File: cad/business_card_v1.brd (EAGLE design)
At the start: 50 x 50 mm, 31 parts, among them SW1 SPST_TACT-KMR2

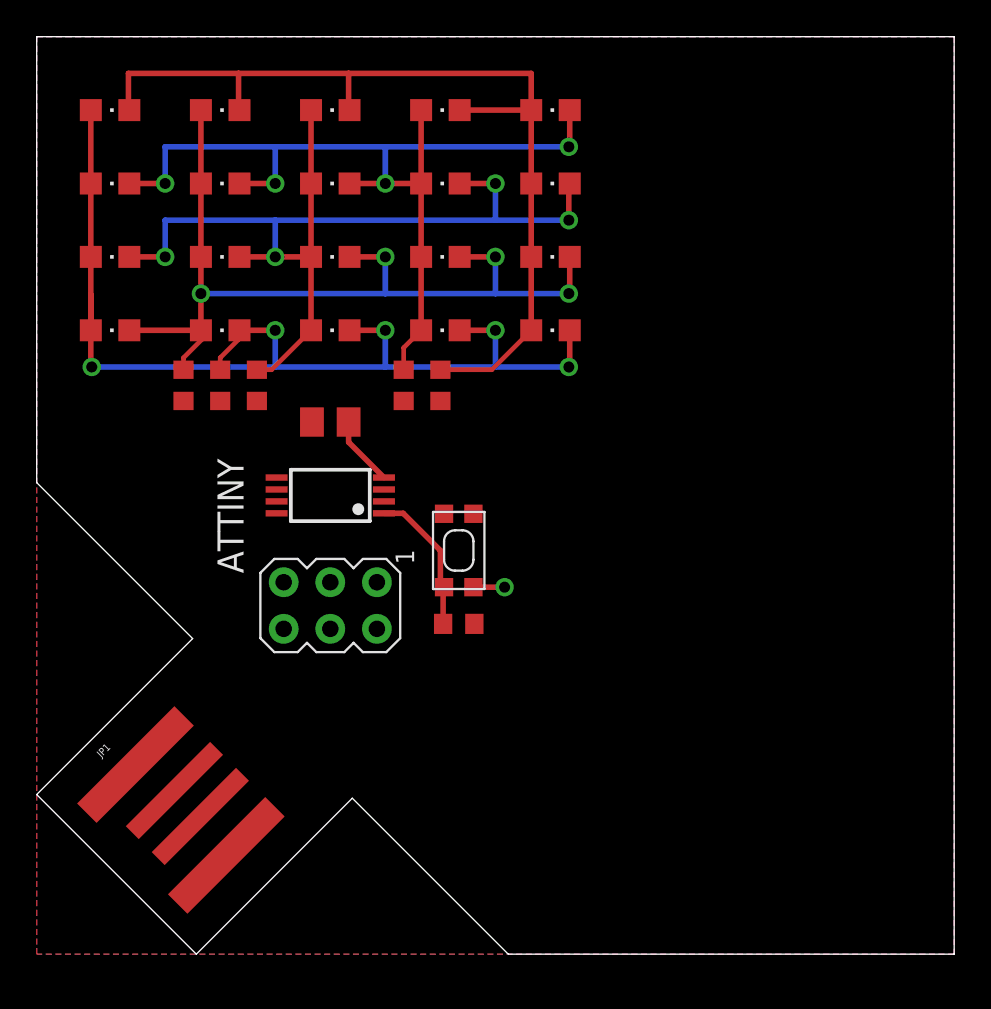
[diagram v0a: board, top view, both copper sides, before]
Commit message: deleted lock on .sch file
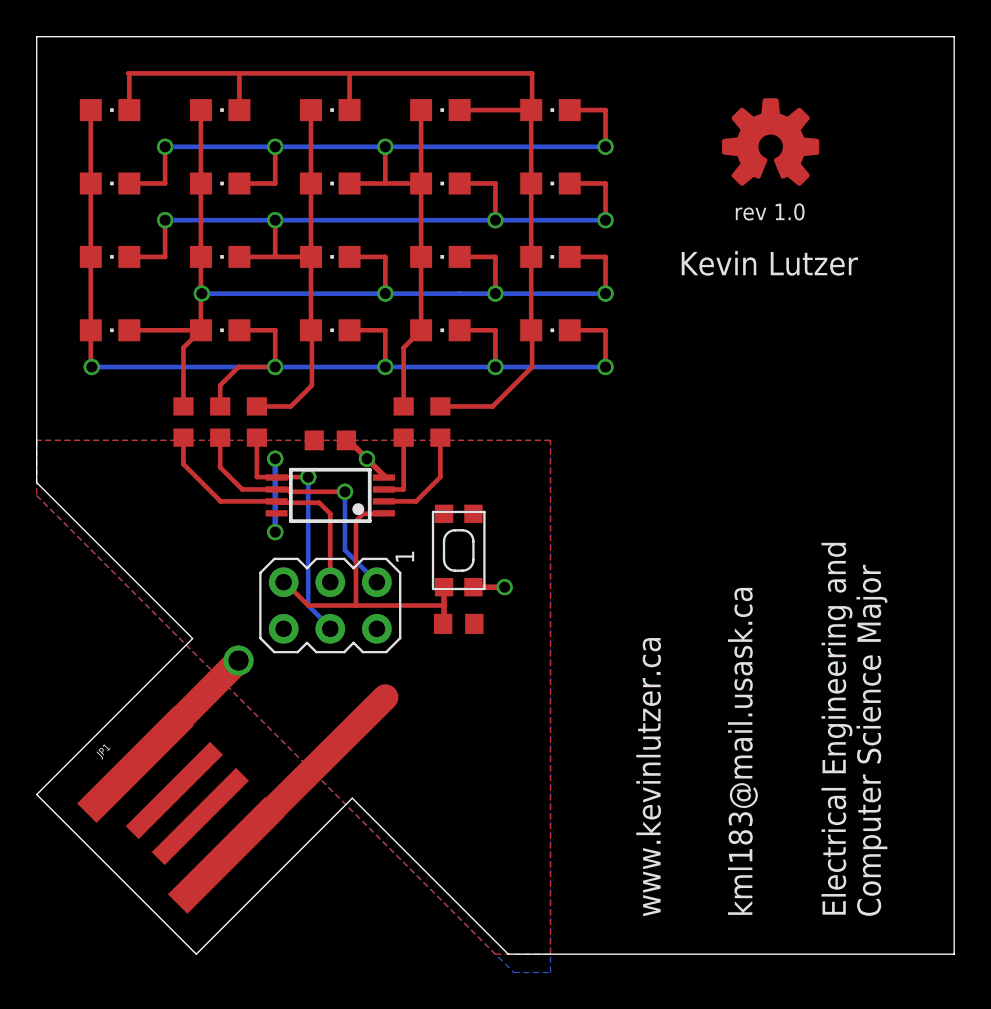
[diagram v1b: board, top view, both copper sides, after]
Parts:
- added U$1: (no value), adafruit:OSHWLOGO_TOP_0.2
- C1: value (none) -> 0.1uF; device resistor:C0805K -> adafruit:C0603K
- moved R2 2.00 mm to (10.0, 29.0)
- moved R3 2.00 mm to (8.00, 29.0)
- moved R4 2.00 mm to (12.0, 29.0)
- moved R5 2.00 mm to (20.0, 29.0)
- moved R6 2.00 mm to (22.0, 29.0)
- moved C1 1.00 mm to (16.0, 28.0)
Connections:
- new net PIN2: ATTINY.7, ISP1.3, R3.1
- new net PIN3: ATTINY.2, R6.1
- new net PIN4: ATTINY.3, R5.1
- net RESET: now also ISP1.5
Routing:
- net +5V: track 0.00 -> 16.2 mm, vias 0 -> 2
- net PIN1: track 0.00 -> 14.6 mm, vias 0 -> 1
- net PIN2: track 0.00 -> 14.4 mm
- net PIN0: track 0.00 -> 13.7 mm, vias 0 -> 1
- net RESET: track 8.02 -> 17.6 mm
- net GND: track 5.52 -> 12.7 mm, vias 1 -> 3
- net N$12: track 53.7 -> 60.2 mm
- net N$13: track 48.5 -> 54.6 mm
- net N$9: track 52.4 -> 58.3 mm
- net PIN3: track 0.00 -> 5.77 mm
- net N$1: track 58.4 -> 62.4 mm
- net PIN4: track 0.00 -> 3.90 mm
- net N$6: track 51.8 -> 53.9 mm
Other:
- board text added: "Electrical Engineering and Computer Science Major"
- board text added: "Kevin Lutzer"
- board text added: "kml183@mail.usask.ca"
- board text added: "rev 1.0"
- board text added: "www.kevinlutzer.ca"
